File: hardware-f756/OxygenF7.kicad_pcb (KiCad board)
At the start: 2 copper layers, 73 x 45 mm, 65 parts, among them J1 Conn_01x04, J10 Micro_SD_Card_Det, J2 USB_C_2.0, J3 JST SH-4, J4 JST ZH-4, J5 Conn_03x08, J6 Conn_01x16, J7 Conn_01x04, J9 1.25mm, SW1 SW_Push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

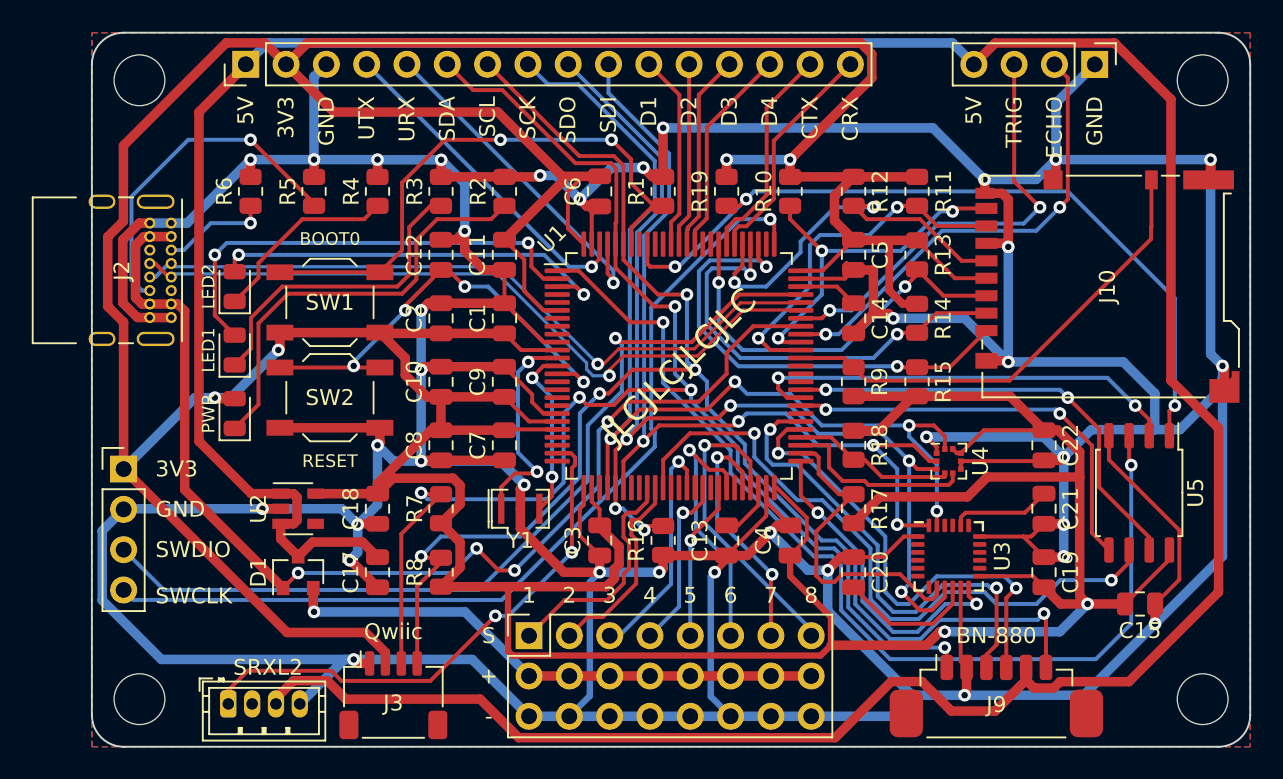
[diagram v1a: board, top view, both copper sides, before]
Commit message: Small layout tweaks
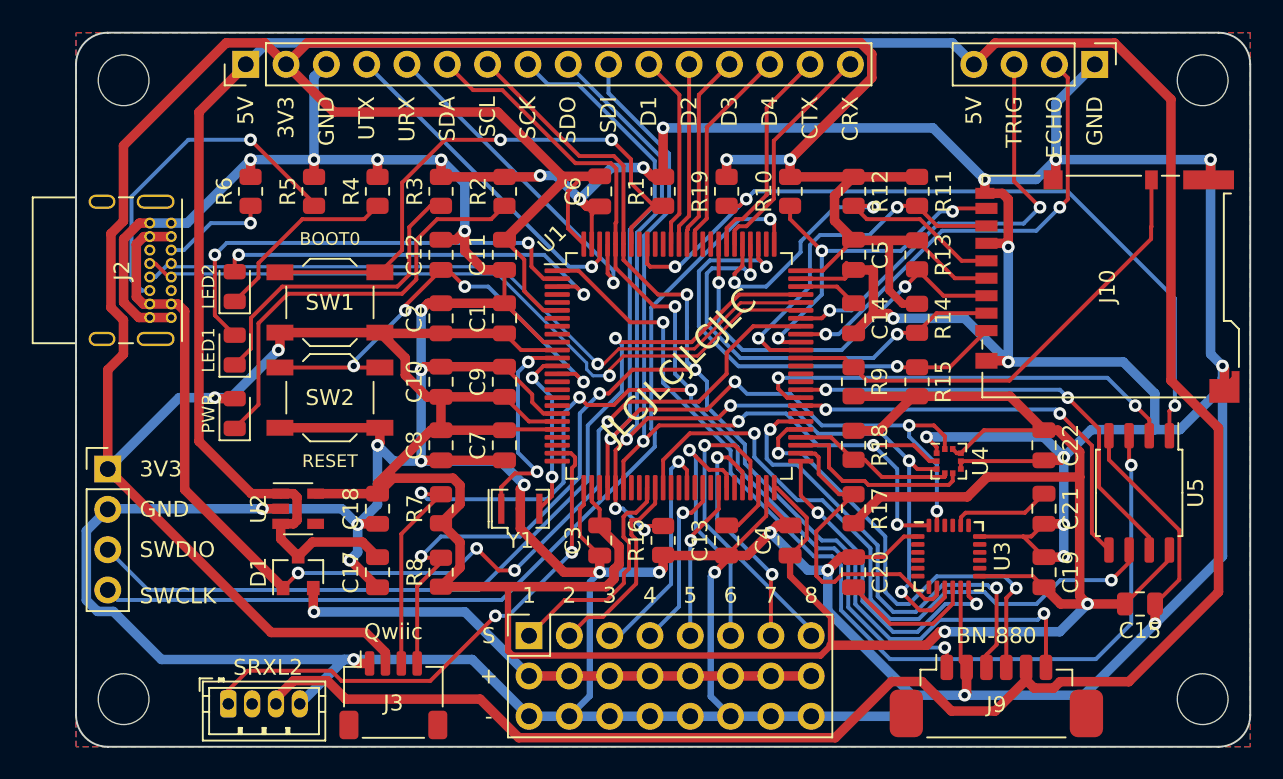
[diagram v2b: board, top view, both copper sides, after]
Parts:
- R2, R4: value 5.1 -> 20
- R3: value 64.9 -> 261
- moved H1 1.00 mm to (116.0, 81.0)
- moved H3 1.00 mm to (116.0, 120.0)
- moved J1 1.00 mm to (115.0, 105.5)
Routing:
- net +3V3: track 401.1 -> 403.3 mm
- net GND: track 512.7 -> 514.6 mm
- net SWDIO: track 57.7 -> 58.7 mm
- net SWCLK: track 58.1 -> 59.1 mm
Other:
- board size 73 x 45 mm -> 74 x 45 mm
